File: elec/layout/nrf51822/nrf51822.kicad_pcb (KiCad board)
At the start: 2 copper layers, 40 x 40 mm, 0 parts

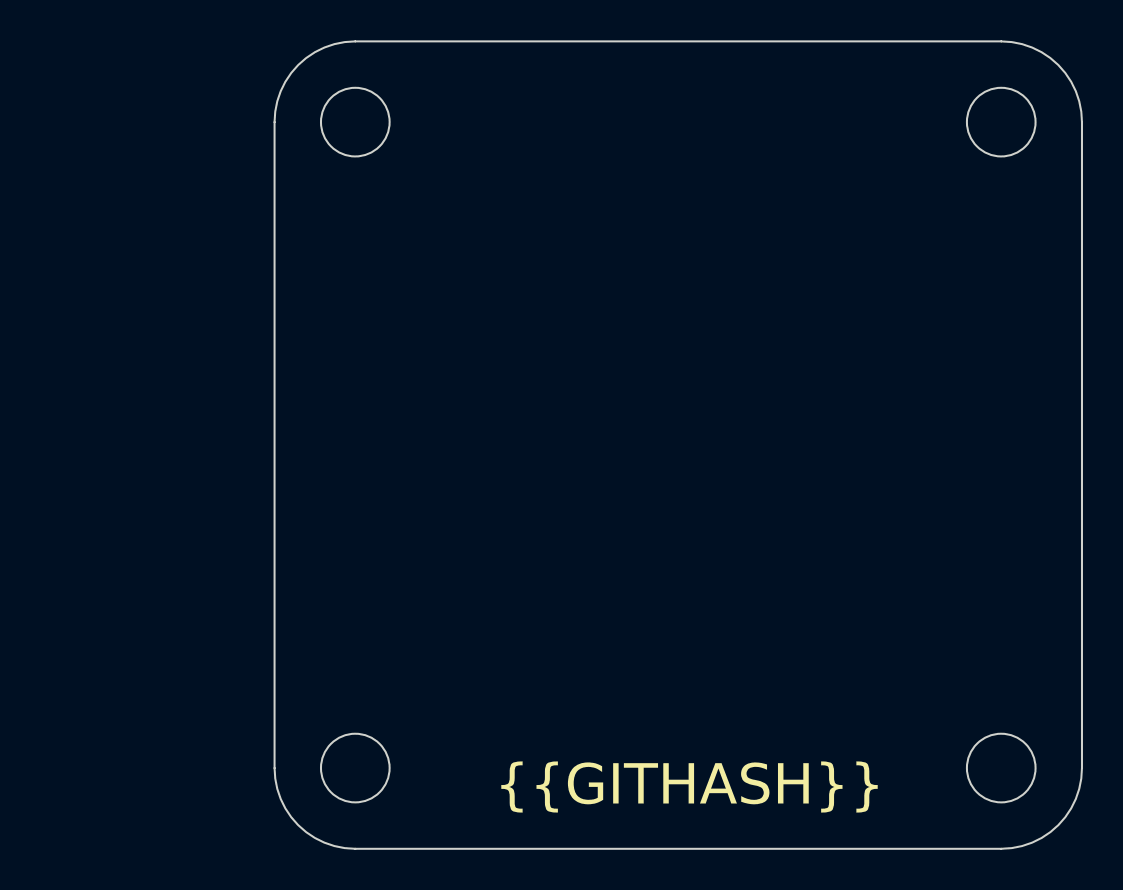
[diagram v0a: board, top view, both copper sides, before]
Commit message: fixed adjacent
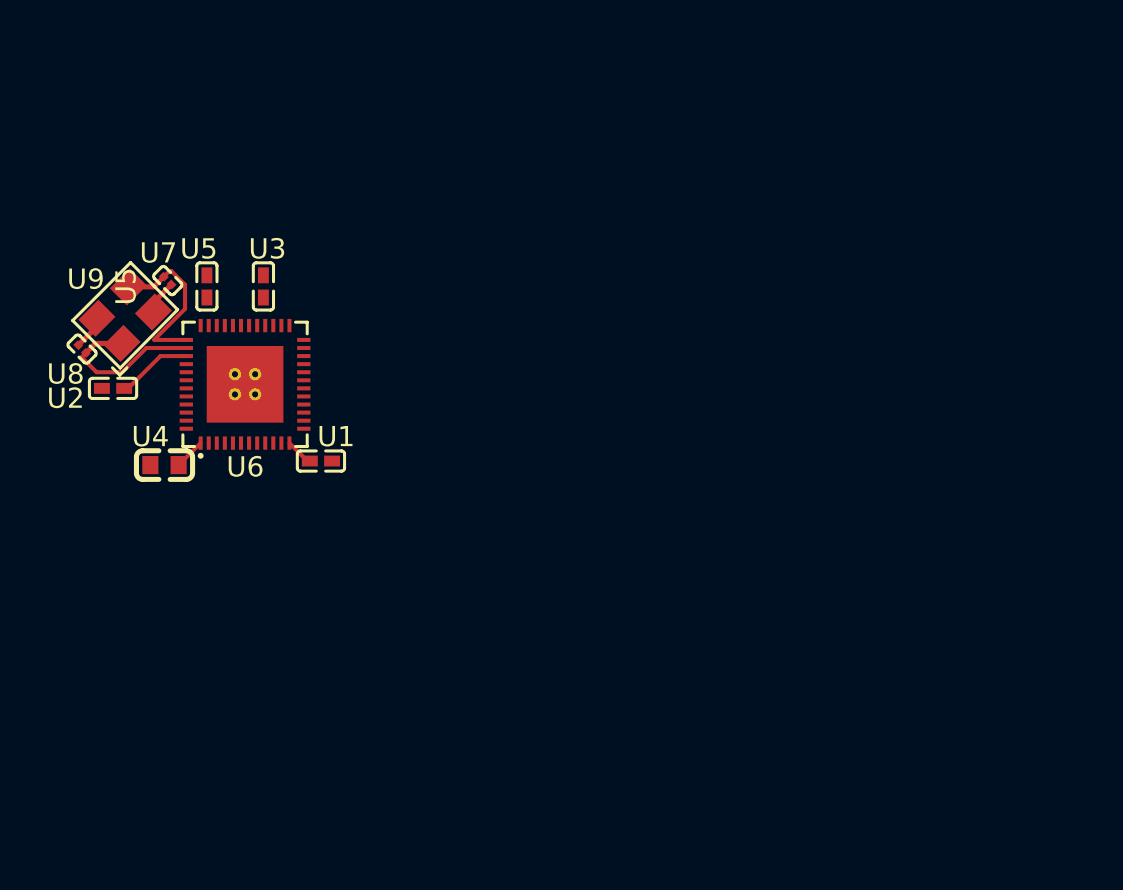
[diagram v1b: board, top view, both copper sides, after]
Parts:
- added U1: 1nF ±10% 50V X7R, atopile:C0402-b3ef17, F.Cu at (131.7, 98.9)
- added U2: 100nF ±10% 16V X7R, atopile:C0402-b3ef17, F.Cu at (121.3, 95.3)
- added U3: 47nF ±10% 50V X7R, atopile:C0402-b3ef17, F.Cu at (128.8, 90.2)
- added U4: 4.7µF ±10% 10V X5R, atopile:C0603-bd72f6, F.Cu at (123.9, 99.1)
- added U5: 100nF ±10% 16V X7R, atopile:C0402-b3ef17, F.Cu at (126.0, 90.2)
- added U6: , lib:QFN-48_L6.0-W6.0-P0.40-BL-EP3.8, F.Cu at (127.9, 95.1)
- added U7: , atopile:C0201-a4ec75, F.Cu at (124.1, 90.0)
- added U8: , atopile:C0201-a4ec75, F.Cu at (119.8, 93.4)
- added U9: , lib:OSC-SMD_4P-L3.2-W2.5-BL, F.Cu at (122.0, 91.7)
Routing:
- net xin: track 0.00 -> 8.36 mm
- net xout: track 0.00 -> 8.28 mm
- net DEC1: track 0.00 -> 3.74 mm
- net gnd: track 0.00 -> 3.46 mm
- net hv: track 0.00 -> 2.92 mm
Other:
- board outline removed
- board text removed: "{{GITHASH}}"
